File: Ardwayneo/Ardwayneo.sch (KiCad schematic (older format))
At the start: 13 parts

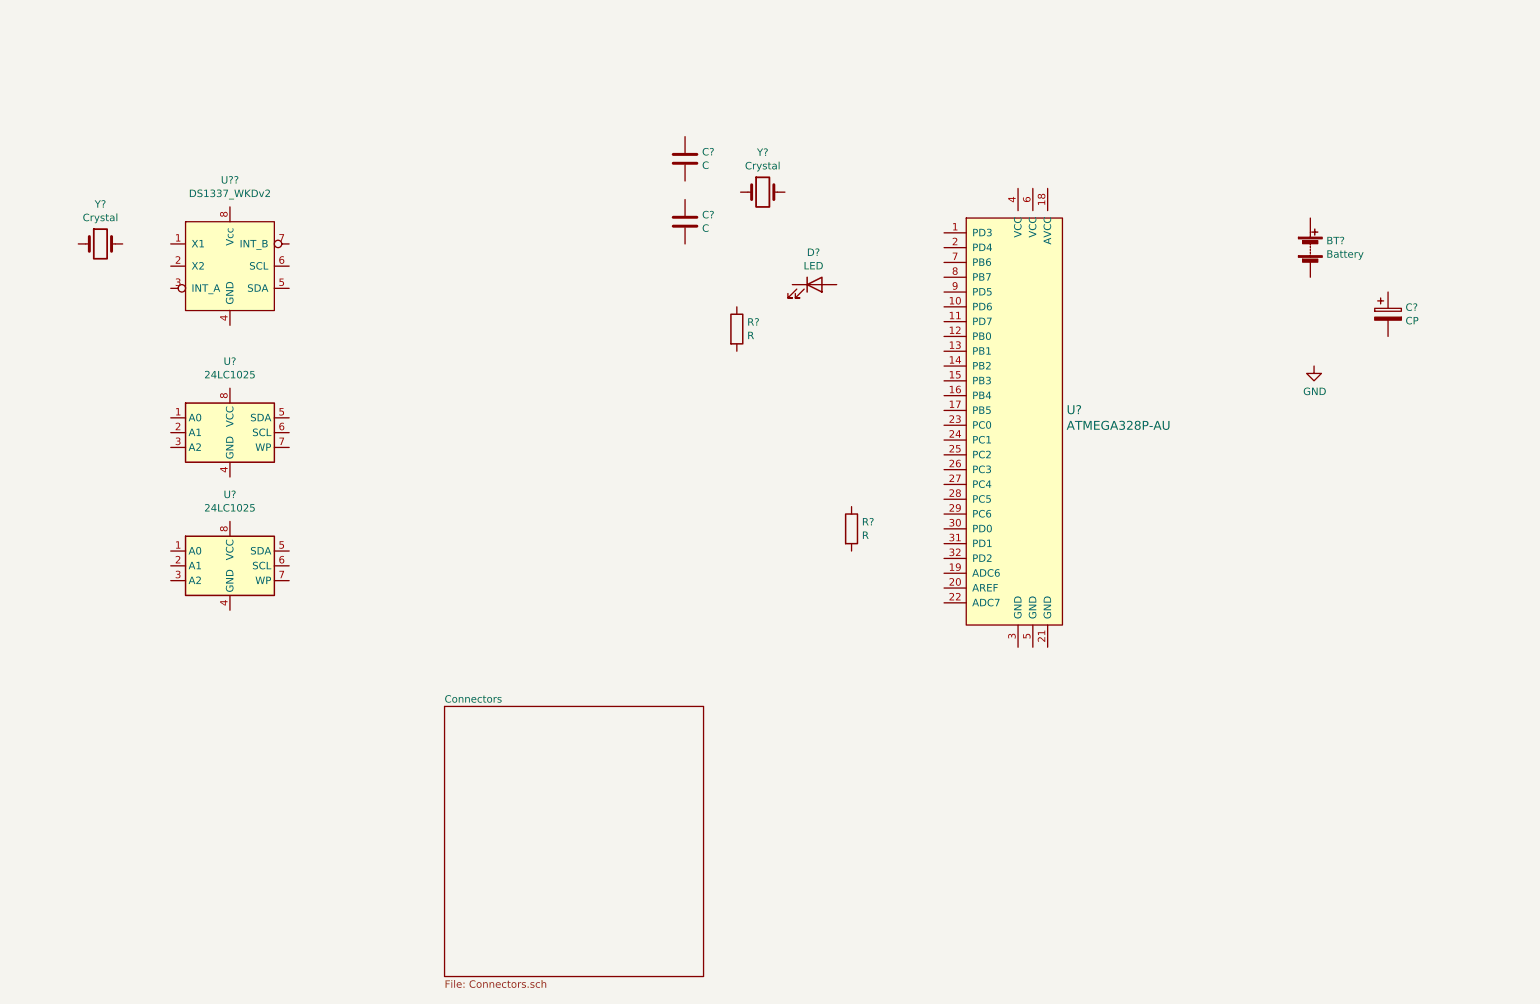
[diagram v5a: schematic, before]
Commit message: Added sheet connector pins to ATMEGA
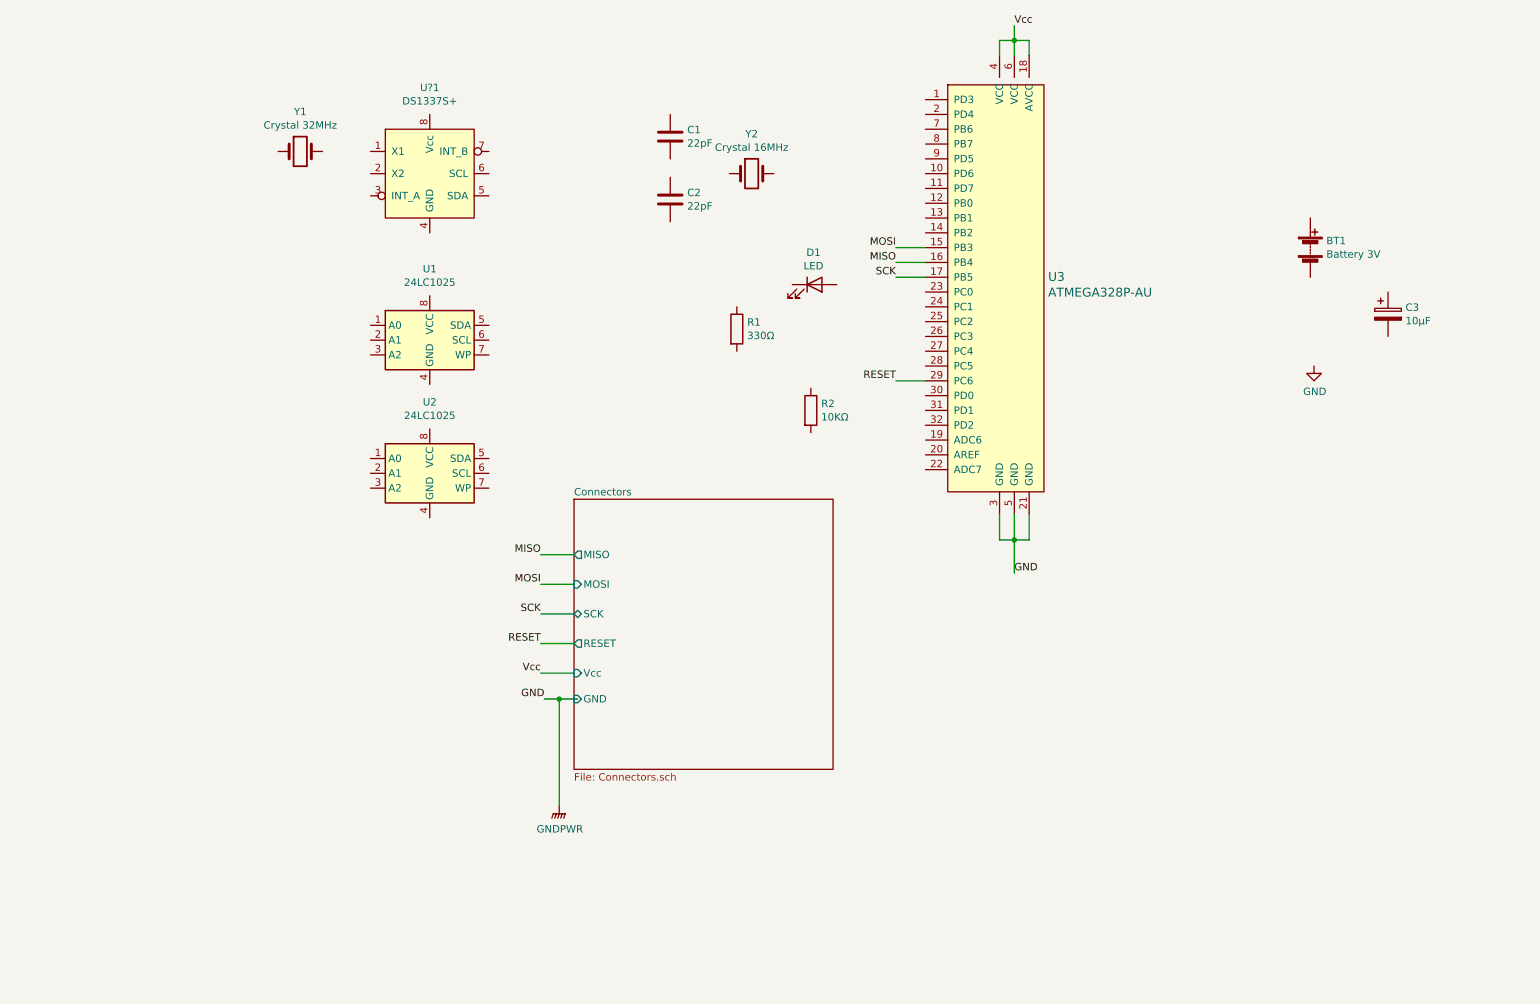
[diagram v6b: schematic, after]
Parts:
- BT1: renamed from BT?; value Battery -> Battery 3V; footprint (none) -> Connector_PinHeader_2.54mm:PinHeader_1x02_P2.54mm_Vertical
- C1, C2: renamed from C?; value C -> 22pF; footprint (none) -> Connector_PinHeader_2.54mm:PinHeader_1x09_P2.54mm_Vertical
- C3: renamed from C?; value CP -> 10µF; footprint (none) -> Connector_PinHeader_2.54mm:PinHeader_1x09_P2.54mm_Vertical
- D1: renamed from D?; footprint (none) -> LED_SMD:LED_0805_2012Metric_Pad1.15x1.40mm_HandSolder
- R1: renamed from R?; value R -> 330Ω; footprint (none) -> Resistor_SMD:R_0805_2012Metric_Pad1.20x1.40mm_HandSolder
- R2: renamed from R?; value R -> 10KΩ; footprint (none) -> Resistor_SMD:R_0805_2012Metric_Pad1.20x1.40mm_HandSolder
- U1, U2: renamed from U?; footprint (none) -> Package_SO:SOIJ-8_5.3x5.3mm_P1.27mm
- U?1: renamed from U??; value DS1337_WKDv2 -> DS1337S+; footprint (none) -> Package_SO:SO-8_5.3x6.2mm_P1.27mm
- Y1: renamed from Y?; value Crystal -> Crystal 32MHz; footprint (none) -> Crystal:Crystal_SMD_MicroCrystal_CC7V-T1A-2Pin_3.2x1.5mm
- Y2: renamed from Y?; value Crystal -> Crystal 16MHz; footprint (none) -> Crystal:Crystal_SMD_5032-2Pin_5.0x3.2mm_HandSoldering
- gave numbers to parts that had none: 1
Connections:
- net labels added: GNDPWR, MISO, MOSI, RESET, SCK, Vcc
- wire segments 0 -> 24
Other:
- moved on the sheet: C1, C2, R2, U1, U2, U3, U?1, Y1, Y2

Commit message: Completed wiring from connectors sheet
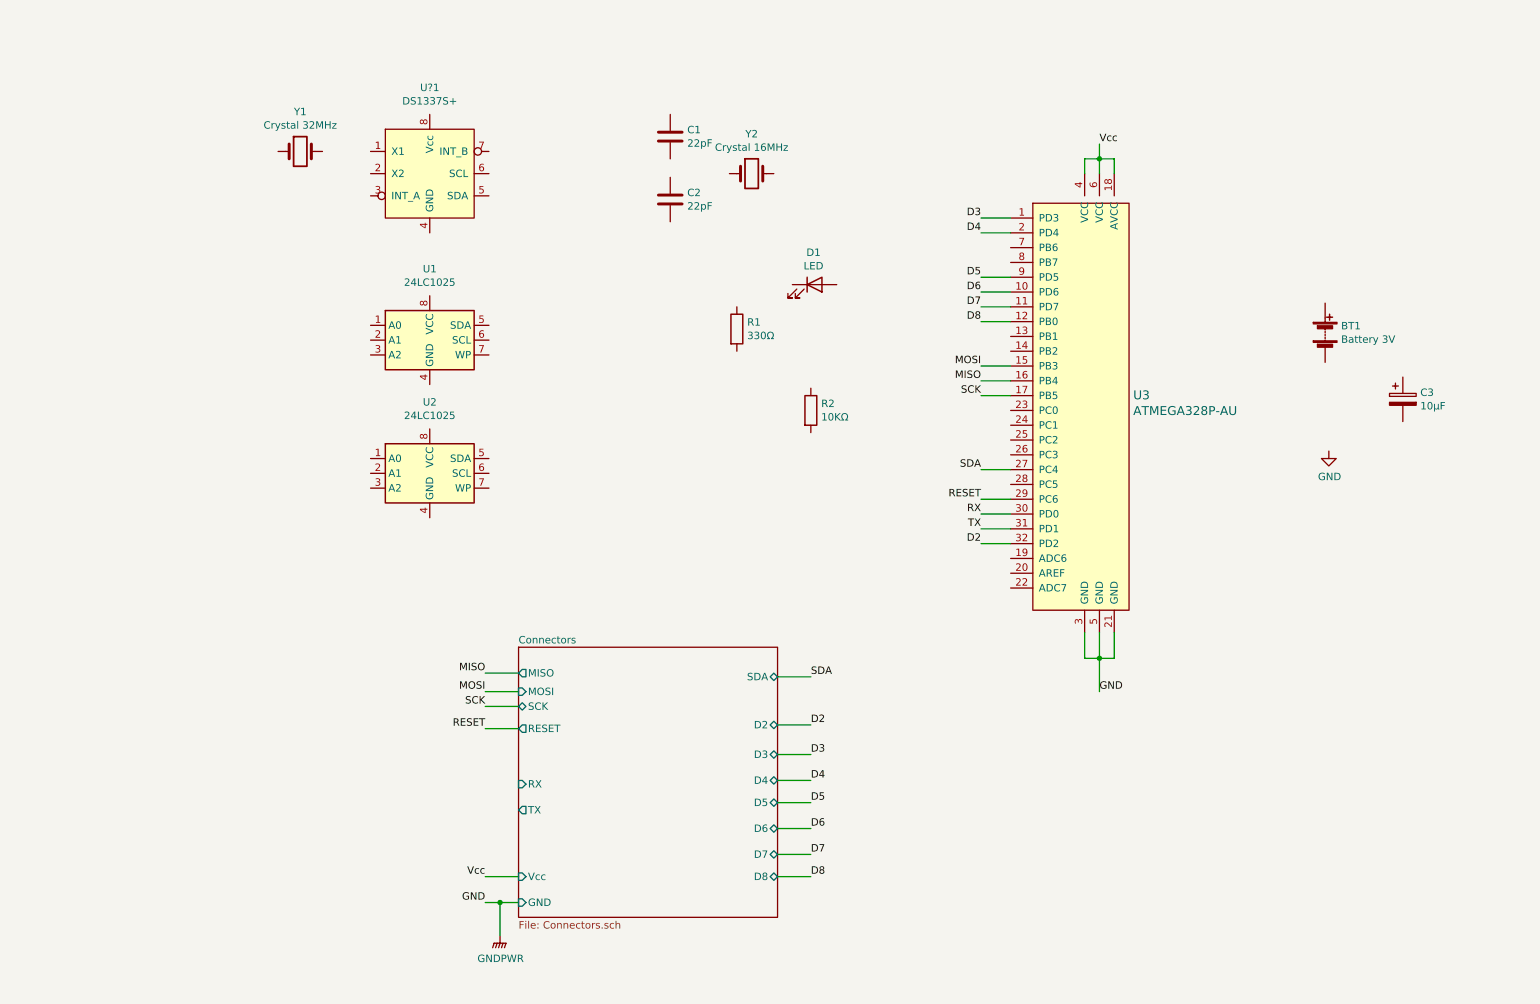
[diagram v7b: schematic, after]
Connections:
- net labels added: D2, D3, D4, D5, D6, D7, D8, RX, SDA, TX
- wire segments 24 -> 42
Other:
- moved on the sheet: BT1, C3, U3

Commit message: Completed wiring root sheet
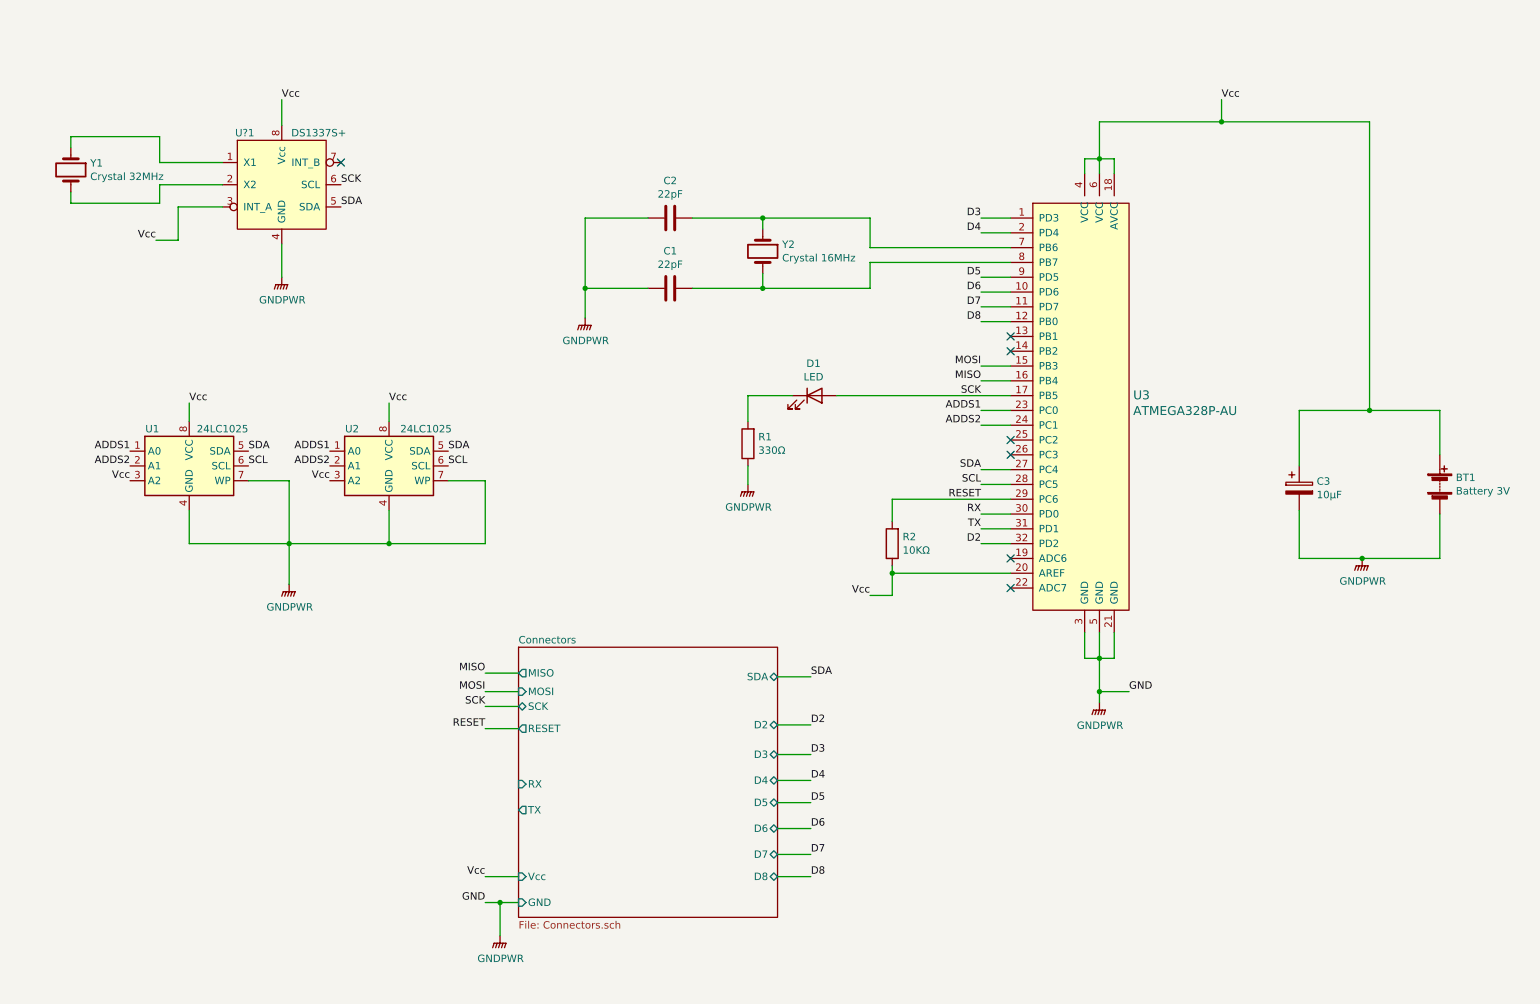
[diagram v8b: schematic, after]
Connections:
- net GND is gone; now on net GNDPWR: U3.21 (GND), U3.3 (GND), U3.5 (GND)
- net RESET: now also R2.2
- net SCK: now also D1.2 (A), U?1.6 (SCL)
- net SDA: now also U1.5 (SDA), U2.5 (SDA), U?1.5 (SDA)
- net Vcc: now also BT1.1 (+), C3.1, R2.1, U1.3 (A2), U1.8 (VCC), U2.3 (A2), U2.8 (VCC), U3.20 (AREF), U?1.3 (INT_A), U?1.8 (Vcc)
- net GNDPWR: now reaches BT1.2 (-)
- net GNDPWR: now also C1.1, C2.2, C3.2, R1.1, U1.4 (GND), U1.7 (WP), U2.4 (GND), U2.7 (WP), U?1.4 (GND)
- net at C1.2: now also U3.8 (PB7), Y2.2
- net at C2.1: now also U3.7 (PB6), Y2.1
- net at D1.1 (K): now also R1.2
- net ADDS1: now reaches U1.1 (A0)
- net ADDS1: now also U2.1 (A0), U3.23 (PC0)
- net ADDS2: now reaches U1.2 (A1)
- net ADDS2: now also U2.2 (A1), U3.24 (PC1)
- net SCL: now reaches U1.6 (SCL)
- net SCL: now also U2.6 (SCL), U3.28 (PC5)
- net at U?1.1 (X1): now also Y1.1
- net at U?1.2 (X2): now also Y1.2
- no-connect marks 0 -> 7
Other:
- moved on the sheet: BT1, C1, C2, C3, D1, R1, R2, U1, U2, U?1, Y1, Y2
